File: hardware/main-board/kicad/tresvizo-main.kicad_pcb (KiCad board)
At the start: 4 copper layers, 46 x 64 mm, 116 parts, among them J101 PANEL_USB, J102 BATTERY, J301 GNSS, J401 TF-015, J402 BOTON, J403 OLED, J404 NTC, J405 IMU, Q101 AO3400A, Q102 AO3401A, Q103 AO3400A, Q401 AO3401A, Q402 AO3400A, SW201 RESET, SW202 BOOT, U101 USBLC6-2SC6, U102 BQ25798RQMR, U103 MAX17048G+T10, U105 TPS62903RPJR, U201 ESP32-S3-WROOM-1-N16R2, U301 TPS63070RNMR, U302 USBLC6-2SC6, U303 USBLC6-2SC6

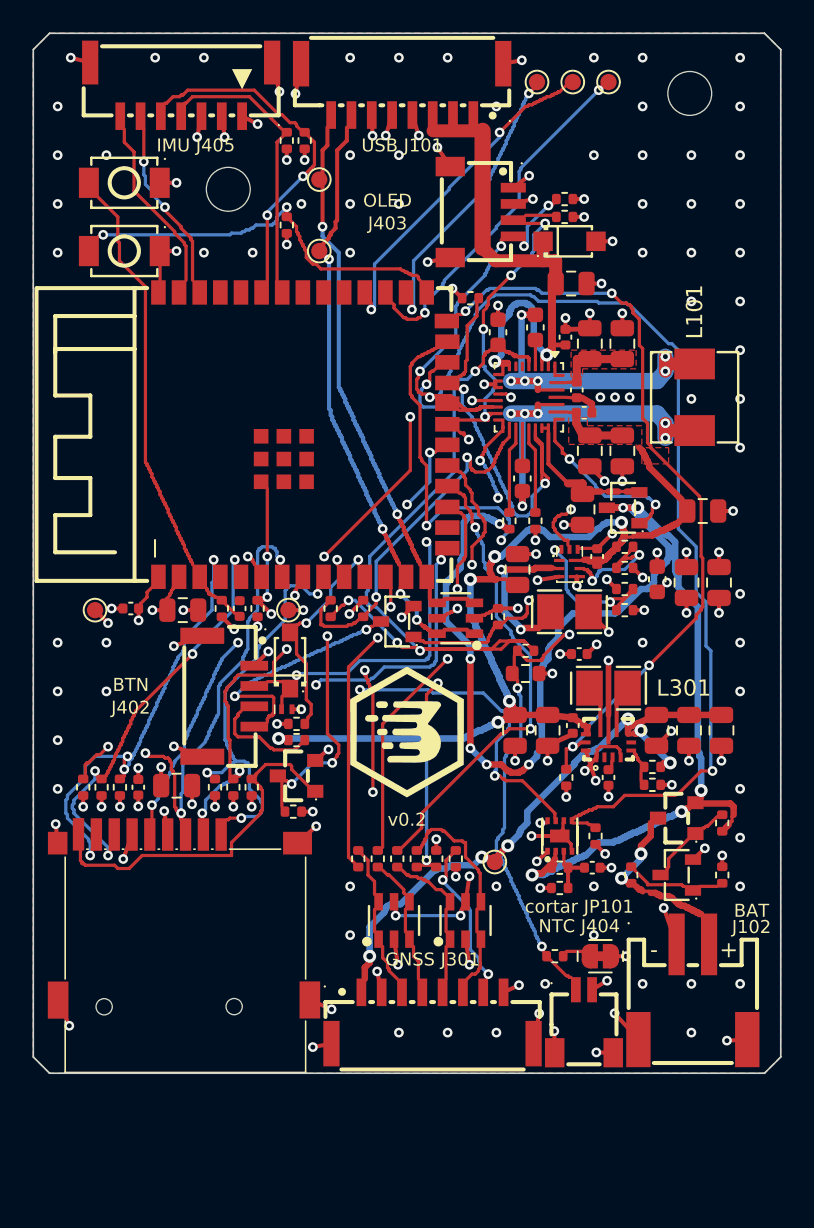
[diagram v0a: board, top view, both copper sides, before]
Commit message: Placa principal v0.2: build reproducible, J301 en SH 8 y montaje en V2.3 con la carrier real
- Build reproducible: kiid_seed.py siembra los KIID de KiCad en cada paso con el contenido de sus
  entradas (sin las líneas de fecha y ruta de la netlist), y route_rest.py toma del DRC solo qué dos
  islas unir y elige siempre los mismos extremos. Dos builds completos dieron los mismos PCB,
  esquemáticos, BOM, CPL, mapa de pines y Gerber; solo cambian las fechas.
- route_rest.py corta los ciclos de arranque (3 por par de conexiones, 20 por conexión en total),
  guarda lo ruteado antes del relleno de zonas y admite ROUTE_FIRST. build.py rutea primero el bus
  de la microSD: con el WROOM, si otras redes toman antes el paso entre el ESP32, J402 y el zócalo,
  SD_CLK y SD_D2 se quedan sin ruta.
- build.py: PYTHONUNBUFFERED, para que un paso que se cae deje sus últimas líneas, y el error dice
  el script y la señal.
- J301 pasa de GH 8 a SH 8 (SM08B-SRSS-TB, C160407; huella de LCSC con anclajes MP y su modelo):
  ya no se puede cruzar con J101, que es GH 8 y lleva VBUS. Va en v 60.7, con la boca en el canto.
  Suma 2.25 USD a los 5 juegos: 209.11 USD.
- Gerber, vistas y esquema en PDF fuera de git salvo en los hitos (.gitignore y nota en los README).
  El quitado del índice quedó por error en b94647d.
- cad/: STEP regenerados con esta placa (modelos de LCSC corregidos por su .wrl) y placement.json al
  día. Nuevo carrier_bdlx.py: la carrier aproximada con sus componentes, sacada de la foto.
  check_montaje_v2_3.py:
  - mueve la placa desplazamiento_placa_y;
  - prueba también la carrier con componentes: encontró los choques de su USB-C y de las soldaduras
    del arnés, que b94647d corrige;
  - lleva el cable de la 18650 1 mm más adelante junto al riel -X.
- ERC 0. DRC con 0 violaciones, 0 sin conectar y 0 de paridad en la placa, la panel-usb y el panel;
  133 de 133 conexiones. Montaje en V2.3 (b94647d) sin choques paso a paso; el cable de la 18650
  pasa libre, a 0.17 mm como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
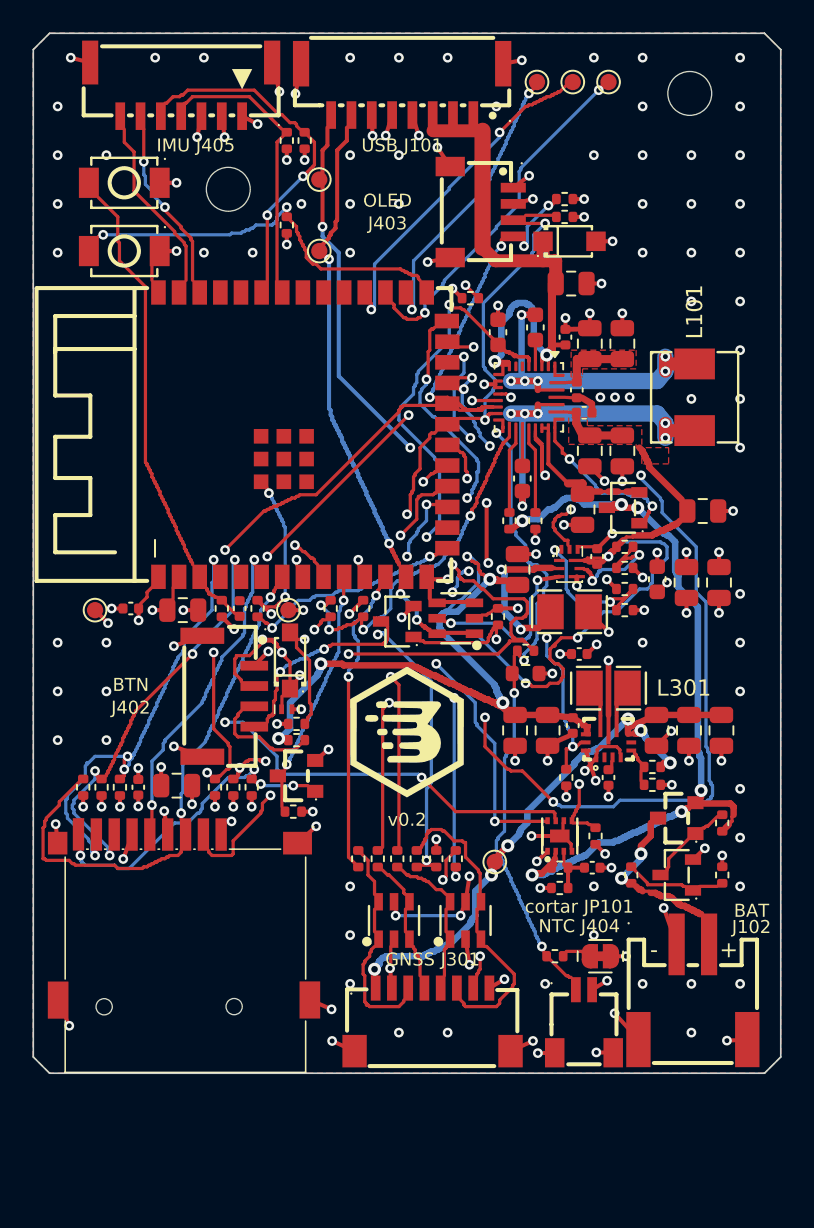
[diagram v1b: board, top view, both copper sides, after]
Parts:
- J301: footprint tresvizo_lcsc:CONN-SMD_8P-P1.25_XUNPU-WAFER-GH1.25-8PWB -> tresvizo_lcsc:CONN-TH_SM08B-SRSS-TB-LF-SN
- moved J301 0.10 mm to (124.6, 160.7)
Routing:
- net /Alimentación, carga y batería/VPACK: track 86.6 -> 48.0 mm, vias 10 -> 6
- net BTN_LED_EN: track 33.8 -> 65.4 mm, vias 3 -> 5
- net FG_ALRT_N: track 62.6 -> 33.8 mm, vias 2 -> 3
- net VSYS: track 65.6 -> 91.1 mm, vias 6 -> 8
- net GNSS_PWR_EN: track 46.8 -> 33.7 mm
- net I2C_SCL: track 69.5 -> 77.8 mm, vias 9 -> 7
- net SD_D3: track 19.7 -> 27.9 mm
- net BTN_N: track 29.6 -> 37.5 mm, vias 3 -> 6
- net /ESP32-S3/ESP_IO3: track 21.2 -> 13.5 mm, vias 3 -> 2
- net USB_DP: track 31.4 -> 38.0 mm, vias 2 -> 5
- net GNSS_PPS_MCU: track 29.0 -> 23.7 mm
- net /GNSS: carrier UM980 por conector y su 5 V/GNSS_EVENT: track 11.3 -> 16.2 mm
- net CHG_TS: track 42.6 -> 38.0 mm, vias 5 -> 4
- net SD_DET: track 19.0 -> 14.7 mm, vias 4 -> 2
- net /GNSS: carrier UM980 por conector y su 5 V/GNSS_RXD2: track 6.60 -> 10.8 mm
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
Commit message: Placa principal v0.2: regulador de 3.3 V (TPS62903) colocado según su hoja de datos
- U105 y sus piezas pasan a la zona libre de la derecha de la placa.
- SW a L102 en 0.9 mm por F.Cu y sin vías. Antes daba un rodeo de 8.7 mm con dos vías y pasaba
  entre los pads de C115.
- C115, el 10 µF de entrada, queda a 0.4 mm de VIN y de GND, con EN saliendo entre sus pads.
- C118 y C119 (salida) junto a la salida de L102 y a GND; VOS toma la tensión en C118.
- FB con su divisor a 1.5 mm: 2.5 mm de pista sin vías (antes 8.6 mm con dos vías).
- Fuera los prerruteos de BUCK_SW y de la vía de GND de U105, que ya no hacen falta.
- ERC 0. DRC con 0 violaciones, 0 sin conectar y 0 de paridad en la placa, la panel-usb y el panel;
  128 de 128 conexiones; dos builds idénticos. Montaje en V2.3 sin choques nuevos.
- README: D+/D- con las cifras del ruteo actual (vienen de una revisión externa).
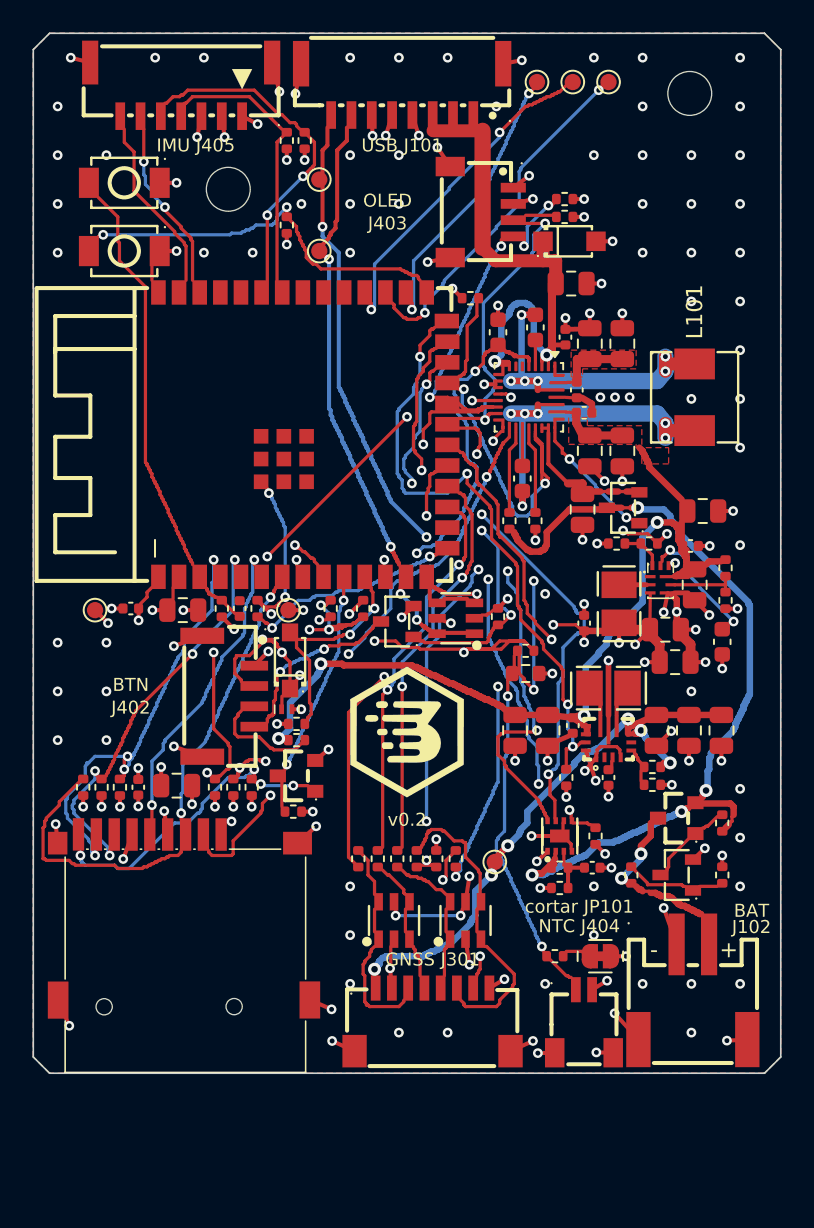
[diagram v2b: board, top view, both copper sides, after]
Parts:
- moved C115 10.9 mm to (140.7, 133.9), turned to -90 degrees
- moved R116 6.51 mm to (142.6, 134.9), turned to -90 degrees
- moved R115 6.33 mm to (142.6, 132.9), turned to -90 degrees
- moved C116 5.79 mm to (140.4, 131.6), turned to 0 degrees
- moved U105 5.69 mm to (138.6, 133.6)
- moved C119 5.59 mm to (139.5, 138.7), turned to 0 degrees
- moved C117 5.55 mm to (142.4, 137.4), turned to -90 degrees
- moved R118 4.37 mm to (137.9, 131.4)
- moved C118 3.18 mm to (138.9, 136.7), turned to 0 degrees
- moved L102 3.09 mm to (136.1, 135.1), turned to -90 degrees
- moved R117 2.84 mm to (135.9, 131.4)
- moved C120 1.92 mm to (133.9, 136.3), turned to 90 degrees
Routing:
- net BTN_LED_EN: track 65.4 -> 25.6 mm, vias 5 -> 3
- net VSYS: track 91.1 -> 56.2 mm, vias 8 -> 4
- net I2C_SCL: track 77.8 -> 56.5 mm
- net GND: track 120.6 -> 130.6 mm, vias 155 -> 157
- net /Alimentación, carga y batería/BUCK_SW: track 8.68 -> 0.95 mm, vias 2 -> 0
- net /Alimentación, carga y batería/CHG_ILIM: track 22.7 -> 29.9 mm, vias 4 -> 5
- net /Alimentación, carga y batería/BUCK_FB: track 8.62 -> 2.47 mm, vias 2 -> 0
- net /Alimentación, carga y batería/REGN: track 53.3 -> 47.5 mm
- net /Alimentación, carga y batería/BUCK_EN: track 8.50 -> 4.13 mm, vias 2 -> 0
- net GNSS_PWR_EN: track 33.7 -> 38.0 mm
- net /Alimentación, carga y batería/BUCK_SS: track 11.4 -> 7.62 mm
- net +3V3: track 44.8 -> 47.6 mm
- net /Alimentación, carga y batería/VPACK: track 48.0 -> 50.6 mm, vias 6 -> 4
- net CHG_TS: track 38.0 -> 40.6 mm, vias 4 -> 5
- net GNSS_RESET_MCU: track 29.4 -> 31.9 mm, vias 5 -> 3
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
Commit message: Placa principal v0.2: NTC de la celda obligatoria en J404
- Fuera R106 (10k fijo) y el puente JP101: TS siempre ve la NTC. Sin NTC enchufada no carga;
  el sistema sigue encendido con el USB.
- Con el divisor 5.1k/30k y una NTC 10k B3435 (103AT), umbrales por omisión del BQ25798 (hoja
  de datos, VT1/TS_COOL/TS_WARM/VT5): no carga bajo ~2 ni sobre ~61 grados, 20 % de corriente
  entre ~2 y 11 y 400 mV menos de voltaje entre ~45 y 61.
- El número R106 queda reservado para no renumerar las demás resistencias.
- README: tabla de temperaturas, aviso de no usar NTC de 100k de impresora 3D y cómo va la NTC
  pegada a la celda en la carcasa V2.3.
- 126 de 126 conexiones; DRC 0, sin conectar 0 y paridad en la placa, la panel-usb y el panel;
  ERC 0. Costo estimado 209.08 USD por 5 juegos.
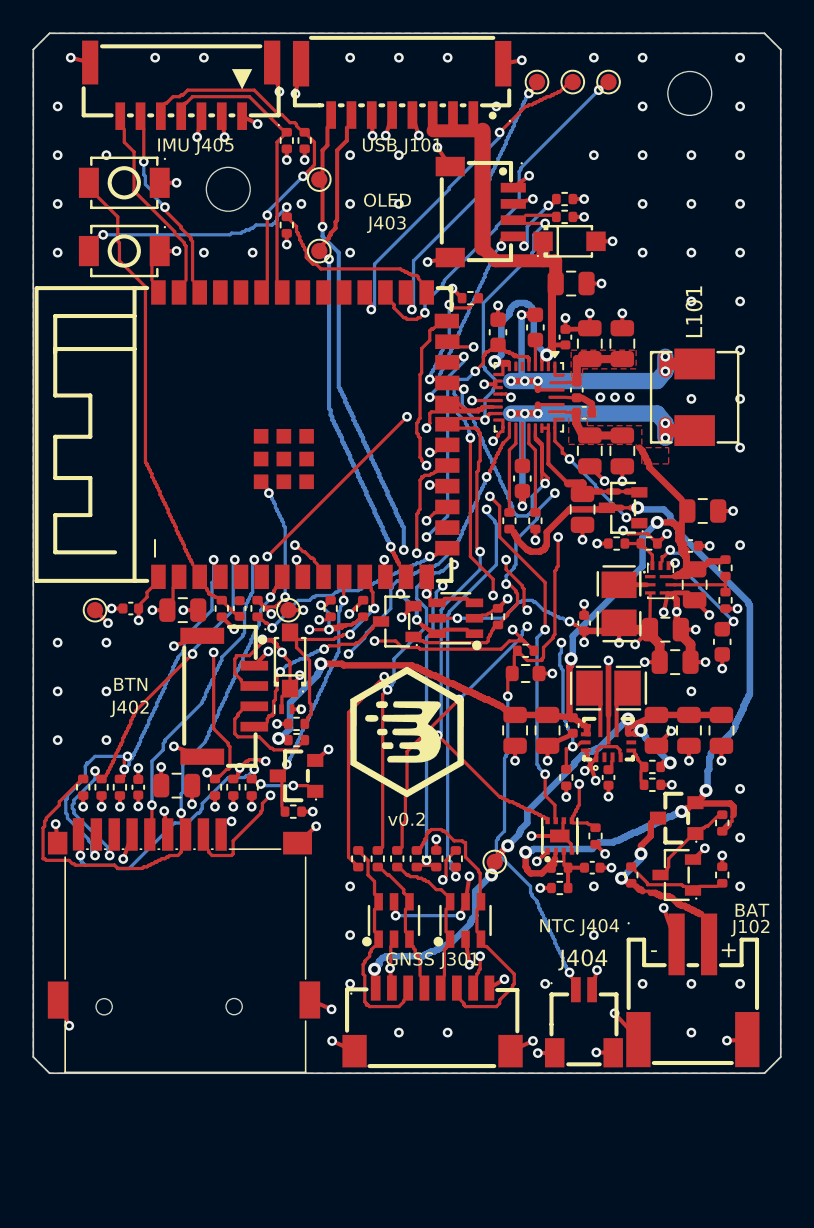
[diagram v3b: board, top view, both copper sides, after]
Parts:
- removed JP101: NTC_CORTAR, tresvizo_lcsc:SolderJumper-2_P1.3mm_Bridged_RoundedPad1.0x1.5mm
- removed R106: 10k, Resistor_SMD:R_0402_1005Metric
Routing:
- net /Alimentación, carga y batería/REGN: track 47.5 -> 41.2 mm, vias 5 -> 6
- net GNSS_PPS_MCU: track 24.0 -> 29.0 mm, vias 2 -> 5
- net GNSS_PWR_EN: track 38.0 -> 33.2 mm, vias 4 -> 3
- net USB_DP: track 37.6 -> 33.2 mm
- net BTN_LED_EN: track 25.6 -> 28.8 mm
- net CHG_INT_N: track 24.7 -> 27.4 mm, vias 2 -> 4
- net GNSS_RESET_MCU: track 31.9 -> 30.1 mm
- net GNSS_TXD2_MCU: track 22.9 -> 24.5 mm, vias 2 -> 3
- net I2C_SCL: track 56.5 -> 55.0 mm, vias 7 -> 8
- net +3V3: track 47.6 -> 48.9 mm
- net /Alimentación, carga y batería/VPACK: track 50.6 -> 51.9 mm
- net CHG_TS: track 40.6 -> 39.4 mm, vias 5 -> 4
- net GNSS_EVENT_MCU: track 27.9 -> 26.8 mm, vias 4 -> 3
- net /Alimentación, carga y batería/CHG_TS_FIJA: track 1.00 -> 0.00 mm
- net GND: track 130.6 -> 129.9 mm, vias 157 -> 155
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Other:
- board text removed: "cortar JP101"
